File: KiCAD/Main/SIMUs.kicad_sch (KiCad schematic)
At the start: 3 parts, among them U11 BMI270, U5 BMI270, U6 BMI270

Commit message: Polish for review
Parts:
- added C14, C15, C16, C17, C18, C19: 100n, symbol Device:C
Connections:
- net SIMU MISO: now reaches U6.1 (SDO)
- net SIMU MISO: now also U11.1 (SDO), U5.1 (SDO)
- net SIMU CS2: now reaches U6.12 (CSB)
- net SIMU CLK: now reaches U6.13 (SCX)
- net SIMU CLK: now also U11.13 (SCX), U5.13 (SCX)
- net SIMU MOSI: now reaches U6.14 (SDX)
- net SIMU MOSI: now also U11.14 (SDX), U5.14 (SDX)
- net SIMU2 INT1: now reaches U6.4 (INT1)
- net +3V3: now reaches U6.5 (VDDIO)
- net +3V3: now also U11.5 (VDDIO), U11.8 (VDD), U5.8 (VDD), U6.8 (VDD), C15.1, C16.1, C17.1, C18.1, C19.1
- net GND: now reaches U6.6 (GNDIO)
- net GND: now also U11.6 (GNDIO), U11.7 (GND), U5.6 (GNDIO), U5.7 (GND), U6.7 (GND), C14.2, C15.2, C16.2, C17.2, C18.2, C19.2
- net SIMU CS3: now reaches U11.12 (CSB)
- net SIMU3 INT1: now reaches U11.4 (INT1)
- net SIMU CS1: now reaches U5.12 (CSB)
- net SIMU1 INT1: now reaches U5.4 (INT1)
- net at U5.5 (VDDIO): now also C14.1

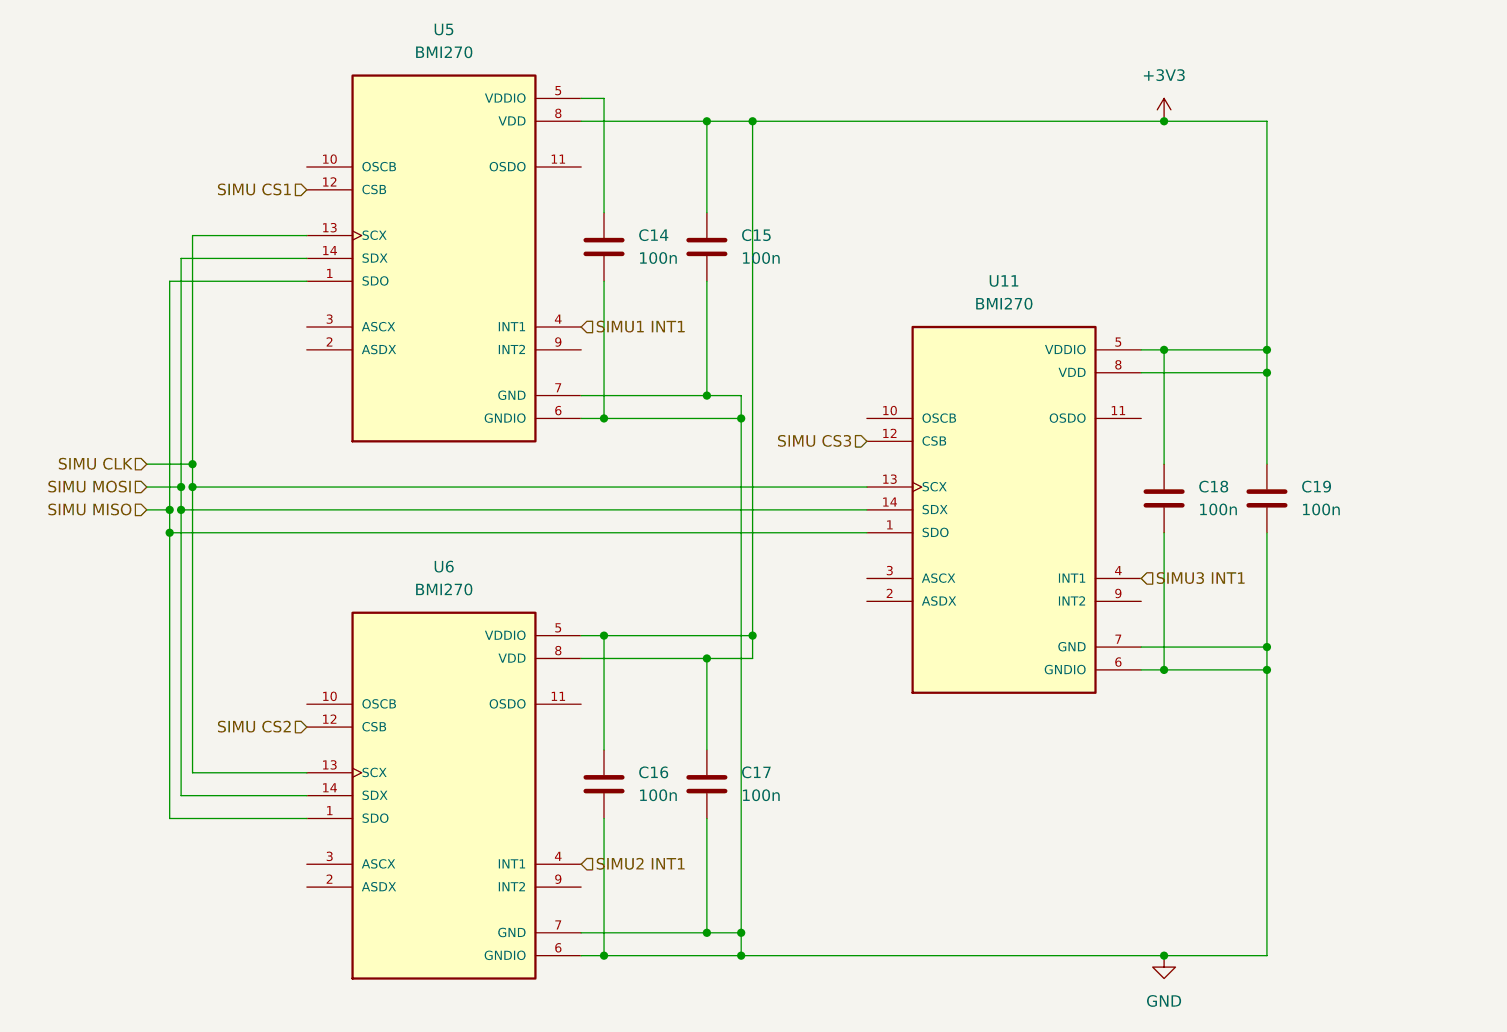
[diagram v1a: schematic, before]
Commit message: Create wiring diagram draft
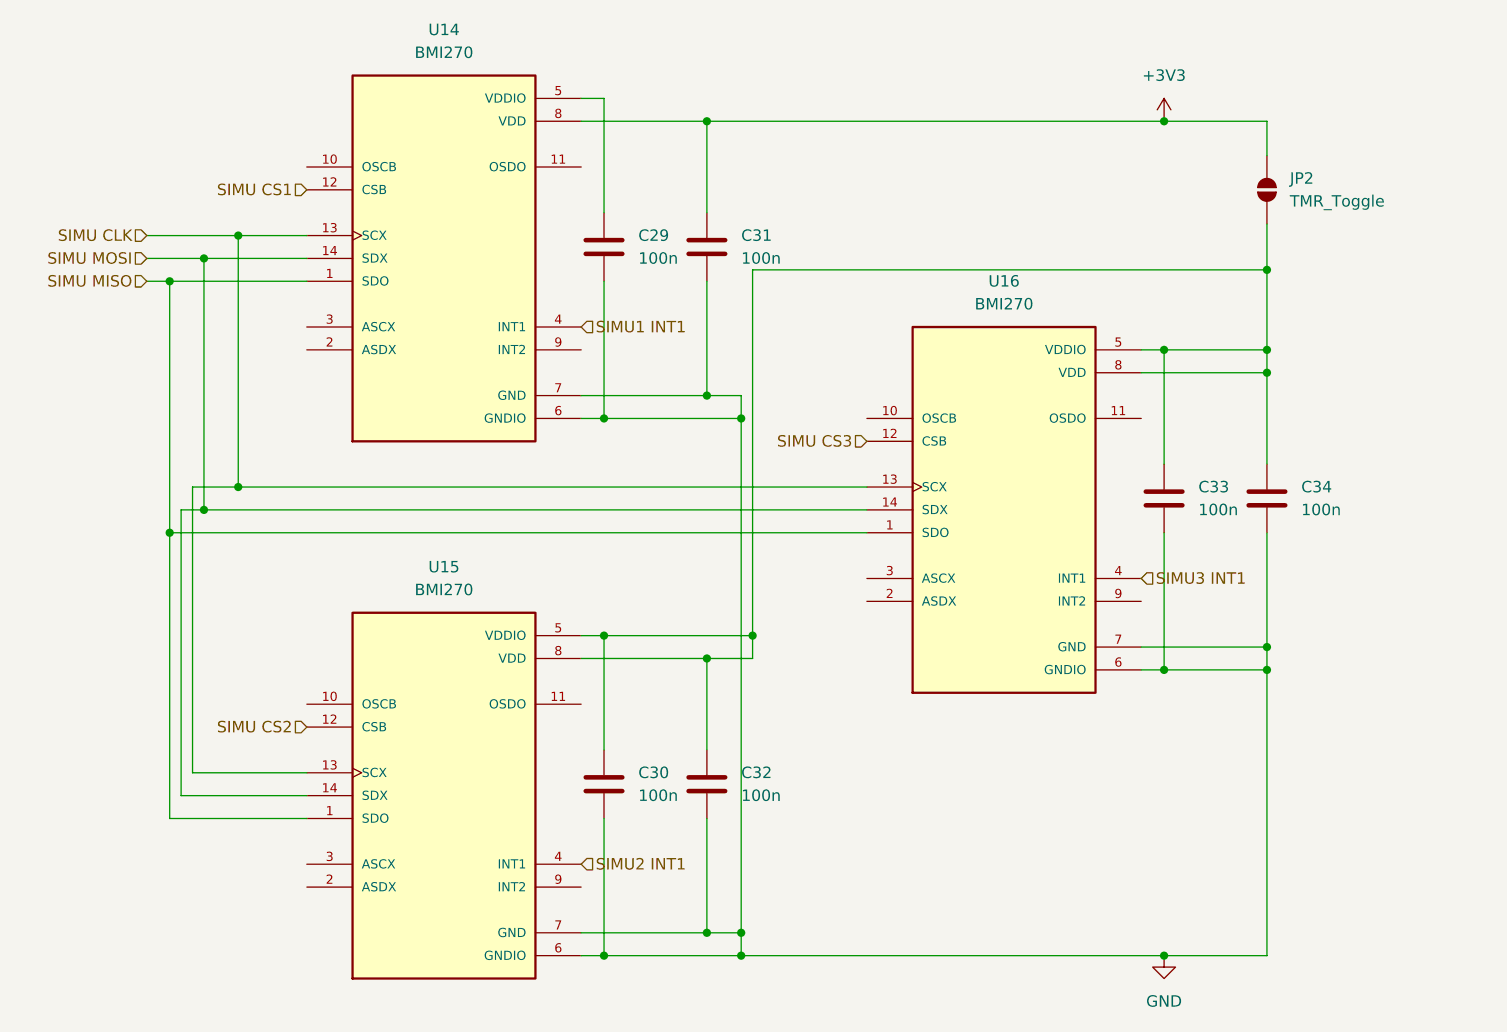
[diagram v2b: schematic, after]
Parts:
- added JP2: TMR_Toggle, symbol Jumper:SolderJumper_2_Open
- renumbered C14 to C29, C16 to C30, C15 to C31, C17 to C32, C18 to C33, C19 to C34, U5 to U14, U6 to U15, U11 to U16
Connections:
- net +3V3: now also JP2.2 (B); no longer C30.1, C32.1, C33.1, C34.1, U15.5 (VDDIO), U15.8 (VDD), U16.5 (VDDIO), U16.8 (VDD)
- new net: C30.1, C32.1, C33.1, C34.1, JP2.1 (A), U15.5 (VDDIO), U15.8 (VDD), U16.5 (VDDIO), U16.8 (VDD)

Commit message: Submit design for review
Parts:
- JP2: value TMR_Toggle -> BMI270 TMR Toggle
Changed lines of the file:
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@@
 		(fields_autoplaced yes)
 		(property "Reference" "JP2"
-			(at 251.46 38.1 90)
+			(at 251.46 38.0999 90)
 			(effects
 				(font
@@
 			)
 		)
-		(property "Value" "TMR_Toggle"
-			(at 251.46 40.64 90)
+		(property "Value" "BMI270 TMR Toggle"
+			(at 251.46 40.6399 90)
 			(effects
 				(font

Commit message: Update RF sys and footprints
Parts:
- C29, C30, C31, C32, C33, C34: footprint (none) -> Capacitor_SMD:C_0603_1608Metric
- JP2: footprint (none) -> Resistor_SMD:R_0603_1608Metric_Pad0.98x0.95mm_HandSolder
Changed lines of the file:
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@@
 			)
 		)
-		(property "Footprint" ""
+		(property "Footprint" "Capacitor_SMD:C_0603_1608Metric"
 			(at 238.4552 77.47 0)
 			(effects
@@
 			)
 		)
-		(property "Footprint" ""
+		(property "Footprint" "Capacitor_SMD:C_0603_1608Metric"
 			(at 187.6552 49.53 0)
 			(effects
@@
 			)
 		)
-		(property "Footprint" ""
+		(property "Footprint" "Capacitor_SMD:C_0603_1608Metric"
 			(at 176.2252 49.53 0)
 			(effects
@@
 			)
 		)
-		(property "Footprint" ""
+		(property "Footprint" "Capacitor_SMD:C_0603_1608Metric"
 			(at 249.8852 77.47 0)
 			(effects
@@
 			)
 		)
-		(property "Footprint" ""
+		(property "Footprint" "Capacitor_SMD:C_0603_1608Metric"
 			(at 187.6552 109.22 0)
 			(effects
@@
 			)
 		)
-		(property "Footprint" ""
+		(property "Footprint" "Capacitor_SMD:C_0603_1608Metric"
 			(at 176.2252 109.22 0)
 			(effects
@@
 			)
 		)
-		(property "Footprint" ""
+		(property "Footprint" "Resistor_SMD:R_0603_1608Metric_Pad0.98x0.95mm_HandSolder"
 			(at 248.92 39.37 0)
 			(effects
